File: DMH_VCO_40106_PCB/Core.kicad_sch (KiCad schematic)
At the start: 45 parts, among them Q1 BC558, Q2 BC548, U1 40106, U2 TL074

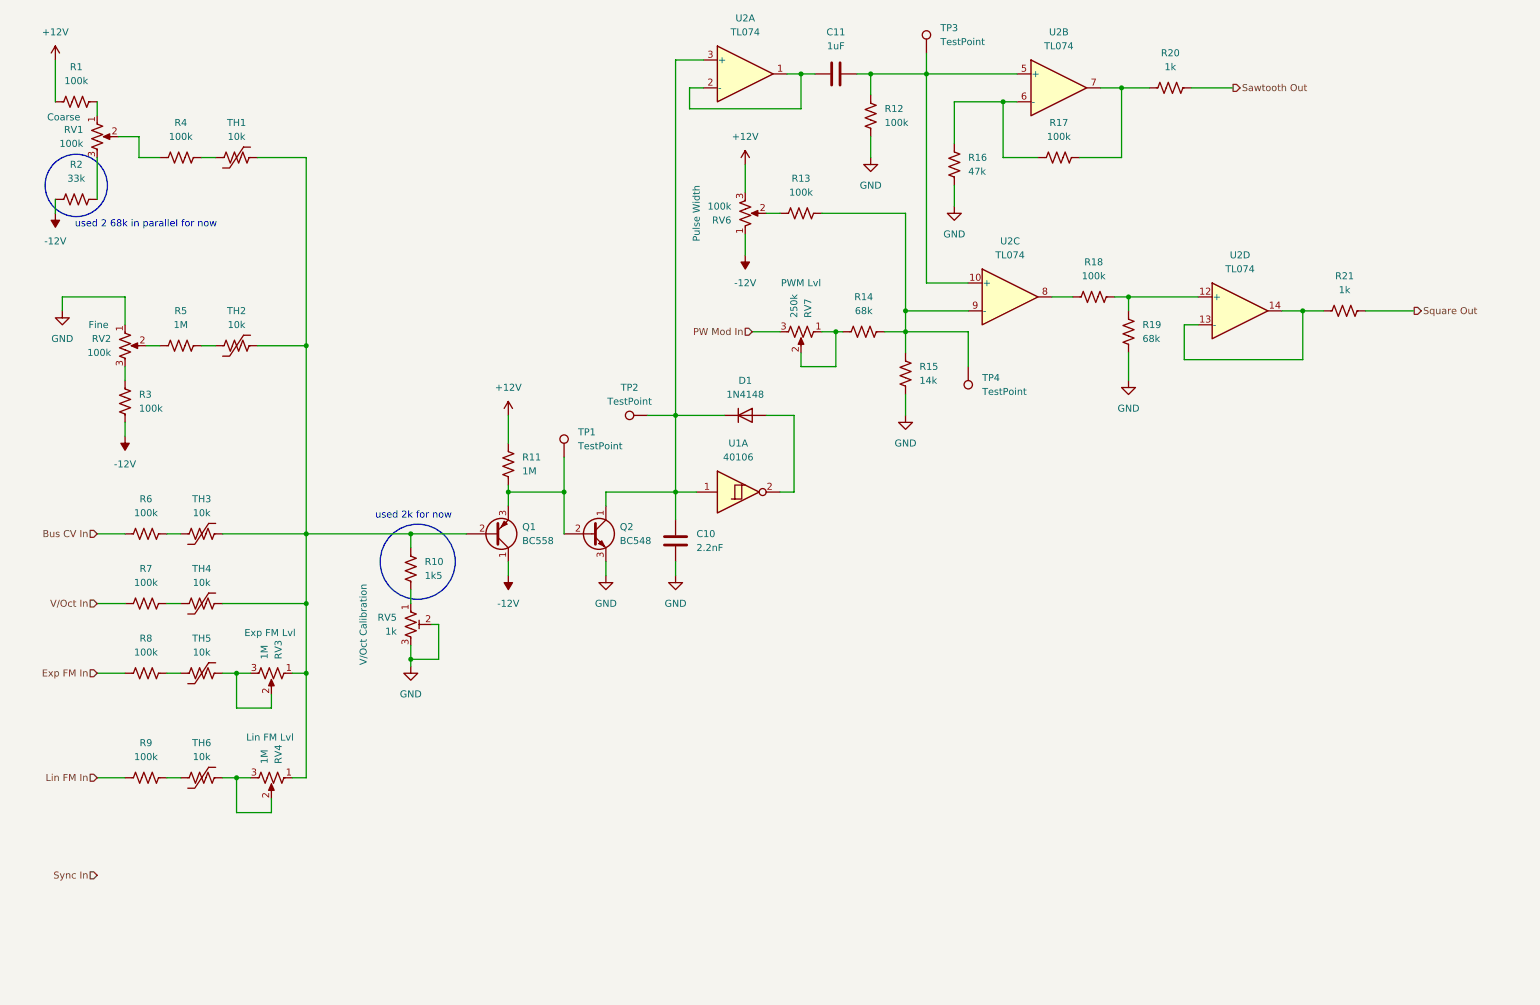
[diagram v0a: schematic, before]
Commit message: Updates from testing on breadboard
- Removed Bus CV input, normalled it to V/oct input jack instead
- Renamed Lin FM input to Exp FM In 2
- Added annotations about temporary resistor/pot values
- Added annotations about pots and trimpots pinout
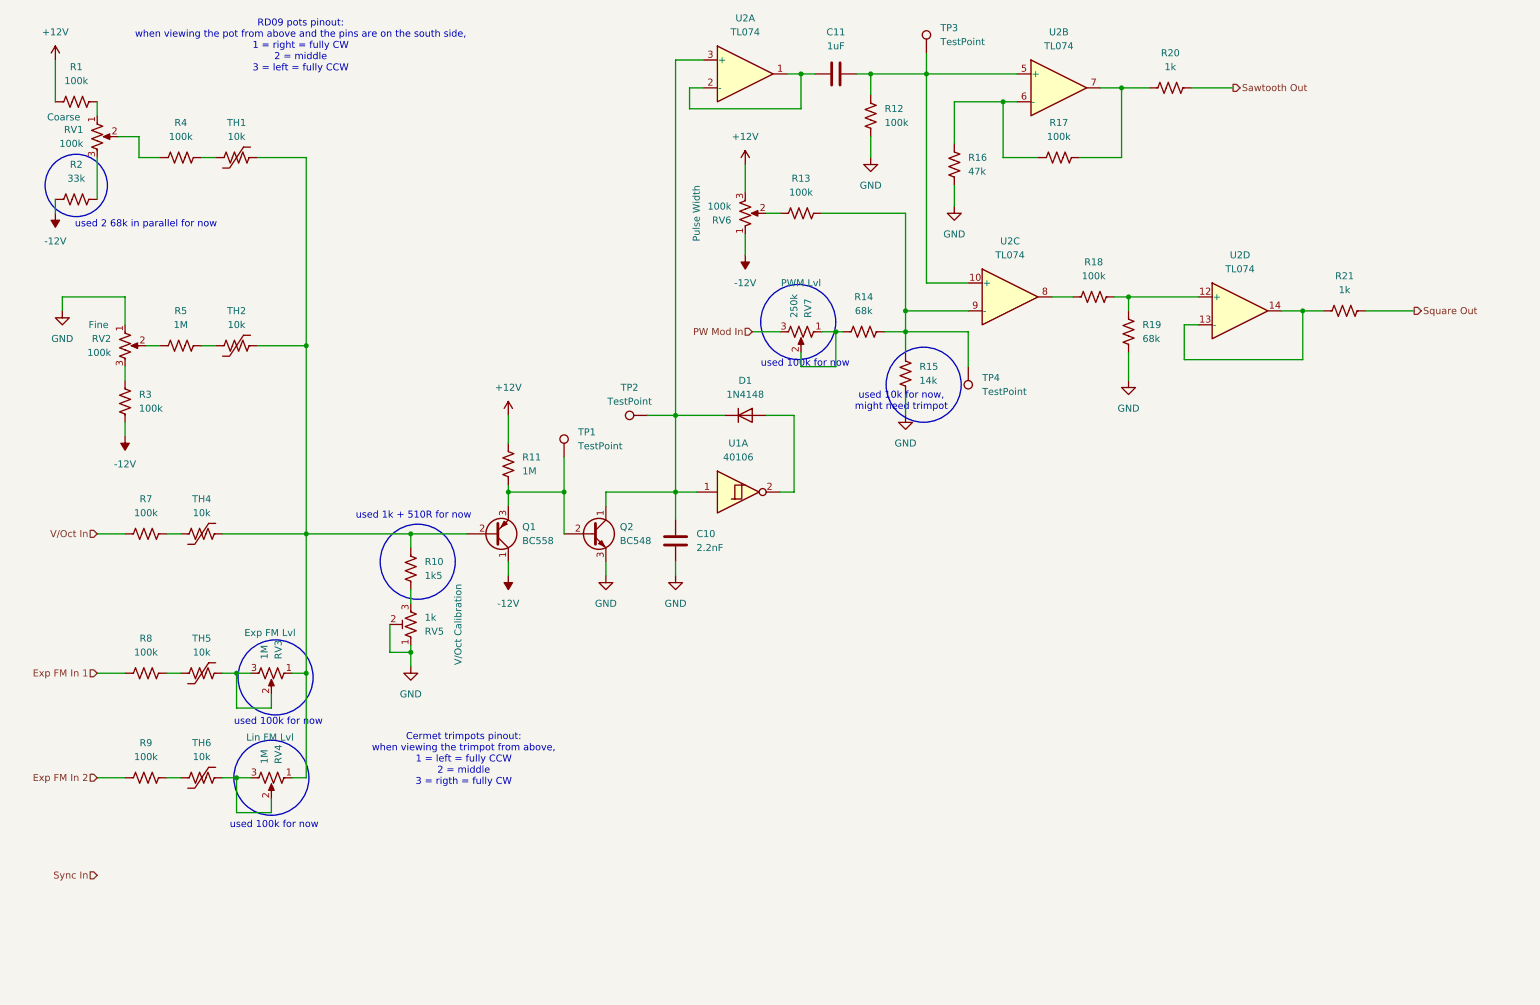
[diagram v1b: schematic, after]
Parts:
- removed R6: 100k, Resistor_THT:R_Axial_DIN0204_L3.6mm_D1.6mm_P5.08mm_Horizontal, symbol Device:R_US
- removed TH3: 10k, Resistor_THT:R_Axial_DIN0204_L3.6mm_D1.6mm_P5.08mm_Horizontal, symbol Device:Thermistor_US
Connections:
- net GND: now also RV5.1; no longer RV5.3
- net at R10.1: now also RV5.3; no longer RV5.1
- net Exp FM In renamed Exp FM In 1
- net Lin FM In renamed Exp FM In 2
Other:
- note added: "Cermet trimpots pinout: when viewing the trimpot from above, 1 = left = fully CCW 2 = middle 3 = rigth = fully CW"
- note added: "RD09 pots pinout: when viewing the pot from above and the pins are on the south side, 1 = right = fully CW 2 = middle 3 = left = fully CCW"
- note added: "used 100k for now"
- note added: "used 10k for now, might need trimpot"
- note added: "used 1k + 510R for now"
- note removed: "used 2k for now"
- company: (none) -> DMH Instruments
- moved on the sheet: R7, RV5, TH4

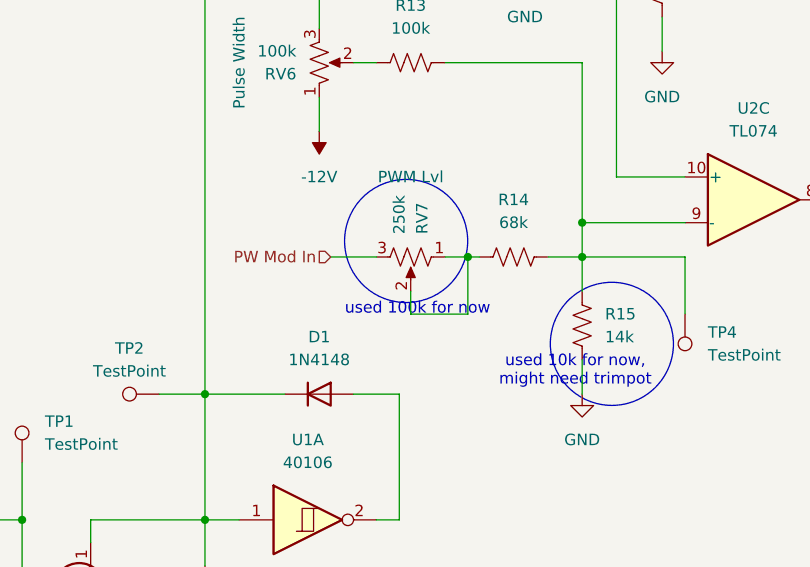
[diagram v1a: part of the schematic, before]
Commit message: Update Core.kicad_sch
- Inverted PW Mod pot orientation.
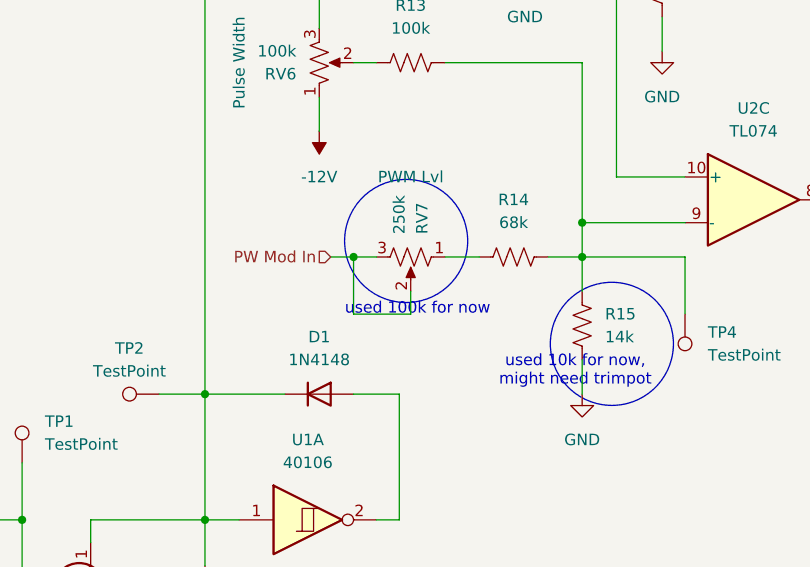
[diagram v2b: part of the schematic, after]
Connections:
- net PW Mod In: now also RV7.2
- net at R14.2, RV7.1: no longer RV7.2
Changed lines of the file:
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@@
-	)
-	(junction
-		(at 160.02 71.12)
-		(diameter 0)
-		(color 0 0 0 0)
 	)
 	(junction
@@
 	)
 	(junction
+		(at 147.32 71.12)
+		(diameter 0)
+		(color 0 0 0 0)
+	)
+	(junction
 		(at 172.72 71.12)
 		(diameter 0)
@@
 	(wire
 		(pts
-			(xy 160.02 77.47) (xy 160.02 71.12)
-		)
-		(stroke
-			(width 0)
-			(type default)
-		)
-	)
-	(wire
-		(pts
 			(xy 63.5 133.35) (xy 63.5 152.4)
 		)
@@
 	(wire
 		(pts
+			(xy 147.32 71.12) (xy 149.86 71.12)
+		)
+		(stroke
+			(width 0)
+			(type default)
+		)
+	)
+	(wire
+		(pts
 			(xy 204.47 39.37) (xy 212.09 39.37)
 		)
@@
 	(wire
 		(pts
-			(xy 160.02 71.12) (xy 161.29 71.12)
-		)
-		(stroke
-			(width 0)
-			(type default)
-		)
-	)
-	(wire
-		(pts
 			(xy 223.52 76.2) (xy 245.11 76.2)
 		)
@@
 	(wire
 		(pts
+			(xy 147.32 77.47) (xy 147.32 71.12)
+		)
+		(stroke
+			(width 0)
+			(type default)
+		)
+	)
+	(wire
+		(pts
 			(xy 130.81 86.36) (xy 130.81 100.33)
 		)
@@
 	(wire
 		(pts
-			(xy 153.67 77.47) (xy 160.02 77.47)
-		)
-		(stroke
-			(width 0)
-			(type default)
-		)
-	)
-	(wire
-		(pts
 			(xy 153.67 74.93) (xy 153.67 77.47)
 		)
@@
 	(wire
 		(pts
-			(xy 157.48 71.12) (xy 160.02 71.12)
+			(xy 157.48 71.12) (xy 161.29 71.12)
+		)
+		(stroke
+			(width 0)
+			(type default)
+		)
+	)
+	(wire
+		(pts
+			(xy 153.67 77.47) (xy 147.32 77.47)
 		)
 		(stroke
@@
 	(wire
 		(pts
-			(xy 144.78 71.12) (xy 149.86 71.12)
-		)
-		(stroke
+			(xy 144.78 71.12) (xy 147.32 71.12)
+		)
+		(stroke

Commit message: Added Cermet 3296W fp to trimpots
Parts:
- RV5: footprint (none) -> Potentiometer_THT:Potentiometer_Bourns_3296W_Vertical
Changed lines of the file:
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@@
 			)
 		)
-		(property "Footprint" ""
+		(property "Footprint" "Potentiometer_THT:Potentiometer_Bourns_3296W_Vertical"
 			(at 82.55 124.46 0)
 			(effects

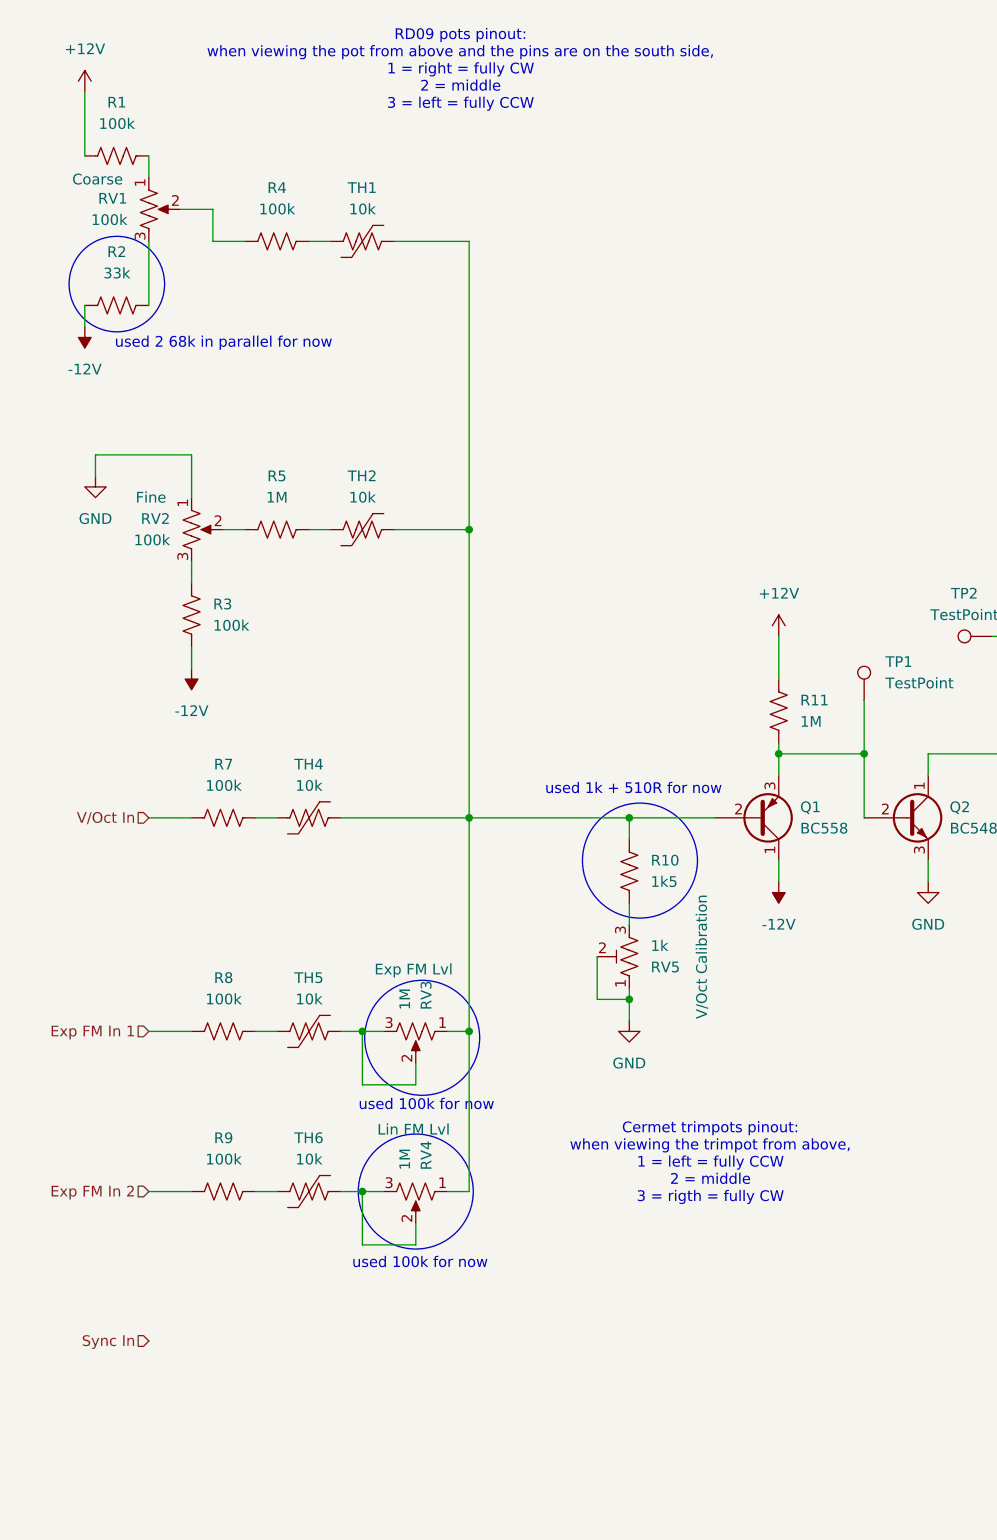
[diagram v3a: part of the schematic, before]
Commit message: Changed Exp FM input attenuator circuitry
Made it so that I can kill the modulation completely when the pot is all de way CCW.
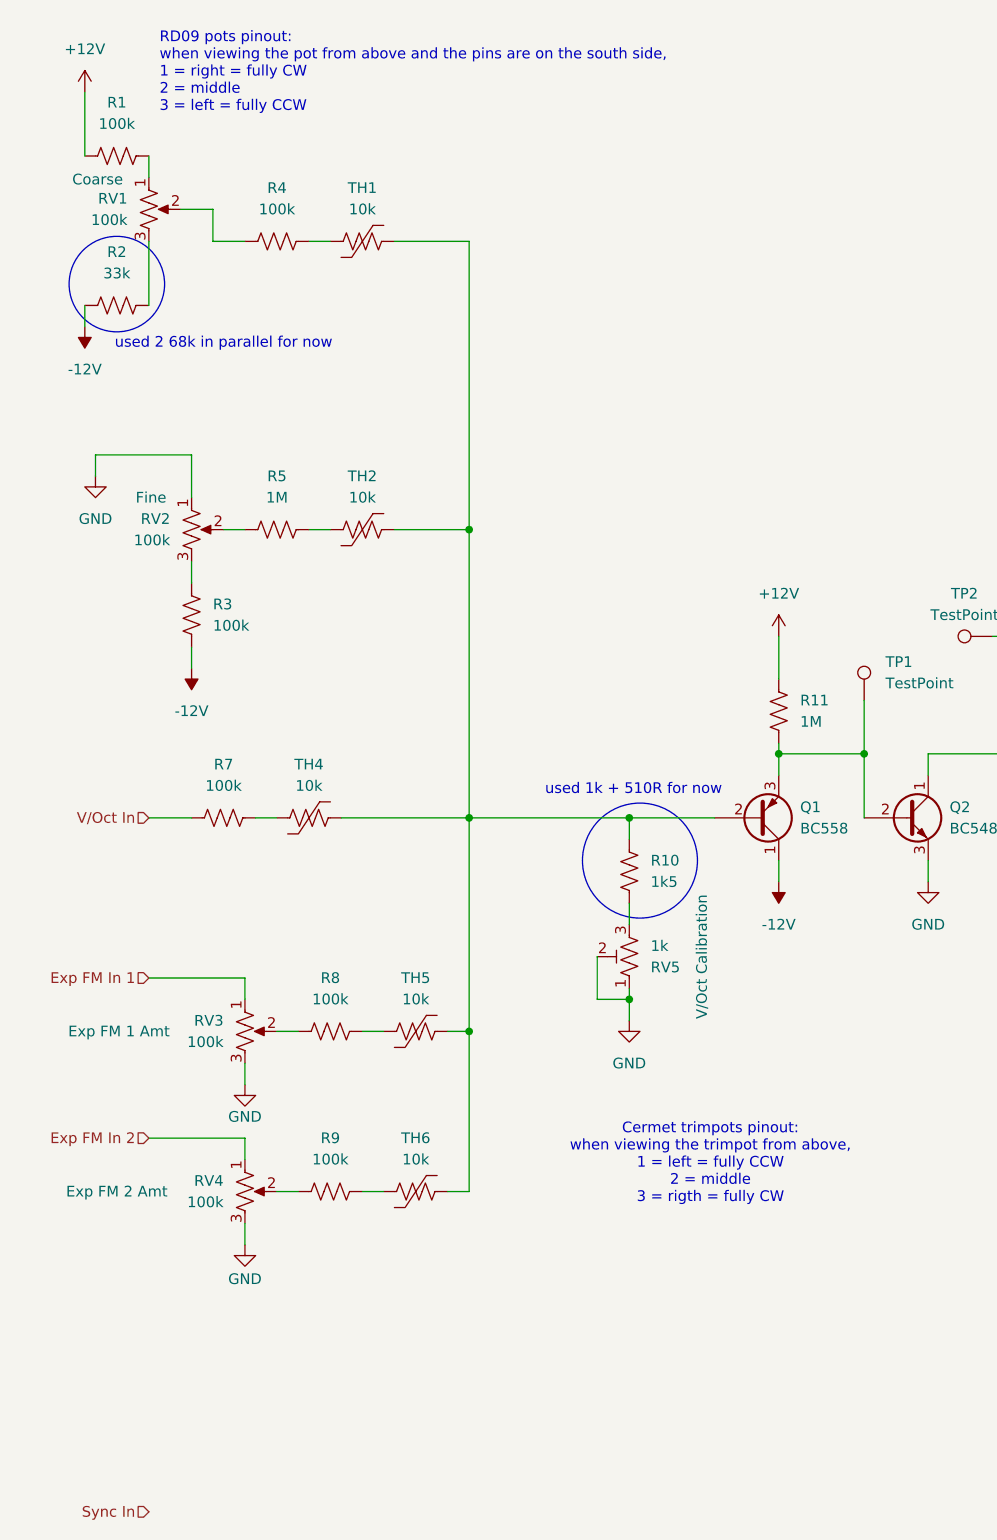
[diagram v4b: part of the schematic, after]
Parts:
- RV3, RV4: value 1M -> 100k
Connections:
- net Exp FM In 1: now also RV3.1; no longer R8.1
- net Exp FM In 2: now also RV4.1; no longer R9.1
- net GND: now also RV3.3, RV4.3
- net at Q1.2 (B), R10.2, TH1.2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: now also TH5.2, TH6.2; no longer RV3.1, RV4.1
- new net: R8.1, RV3.2
- new net: R9.1, RV4.2
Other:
- moved on the sheet: R8, R9, RV3, RV4, TH5, TH6
